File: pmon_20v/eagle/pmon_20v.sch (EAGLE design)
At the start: 34 parts, among them J1 USB, J2 MOLEX 43650-0200, J3 MOLEX 43650-0200, J4 PINHD-2X3, Q1 16Mhz, U1 LTC2943, U2 FT232RL, U3 ATMEGA328TQFP32, U4 TA48M04F

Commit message: Performed final routing.
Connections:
- net +5V renamed VIN
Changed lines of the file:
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@@
 </segment>
 </net>
-<net name="+5V" class="0">
+<net name="VIN" class="0">
 <segment>
 <wire x1="17.78" y1="205.74" x2="35.56" y2="205.74" width="0.4064" layer="91"/>

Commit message: Final tweaks.
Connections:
- net N$22 renamed VOUT
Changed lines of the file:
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@@
 <pinref part="GND21" gate="1" pin="GND"/>
 <pinref part="J2" gate="-2" pin="S"/>
+<label x="-2.54" y="190.5" size="1.778" layer="95"/>
 </segment>
 <segment>
@@
 <wire x1="55.88" y1="190.5" x2="55.88" y2="185.42" width="0.4064" layer="91"/>
 <pinref part="J3" gate="-2" pin="S"/>
+<label x="58.42" y="190.5" size="1.778" layer="95"/>
 </segment>
 <segment>
@@
 <pinref part="R4" gate="G$1" pin="I2"/>
 <pinref part="J2" gate="-1" pin="S"/>
+<label x="-2.54" y="200.66" size="1.778" layer="95"/>
 </segment>
 <segment>
@@
 </segment>
 </net>
-<net name="N$22" class="0">
+<net name="VOUT" class="0">
 <segment>
 <wire x1="48.26" y1="205.74" x2="55.88" y2="205.74" width="0.4064" layer="91"/>
@@
 <pinref part="R4" gate="G$1" pin="I1"/>
 <pinref part="J3" gate="-1" pin="S"/>
-</segment>
-</net>
+<label x="58.42" y="200.66" size="1.778" layer="95"/>
+</segment>
+</net>

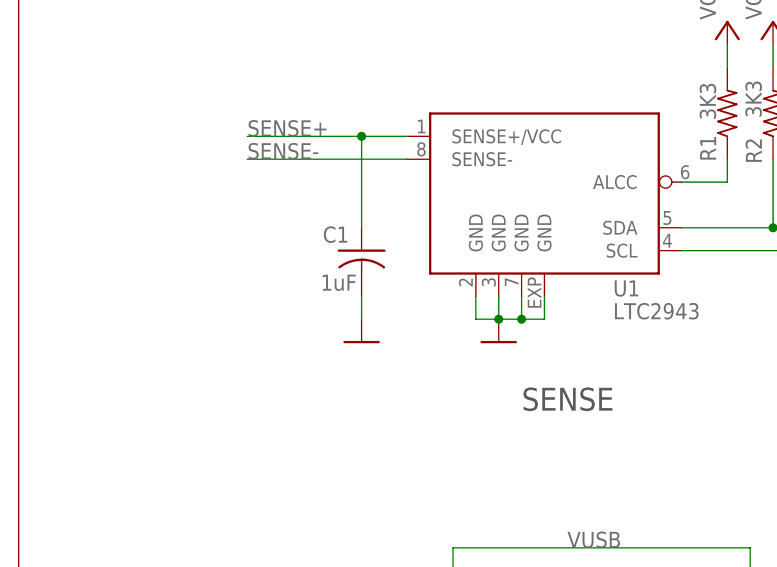
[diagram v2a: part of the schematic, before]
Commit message: Added covers for pmon 20V
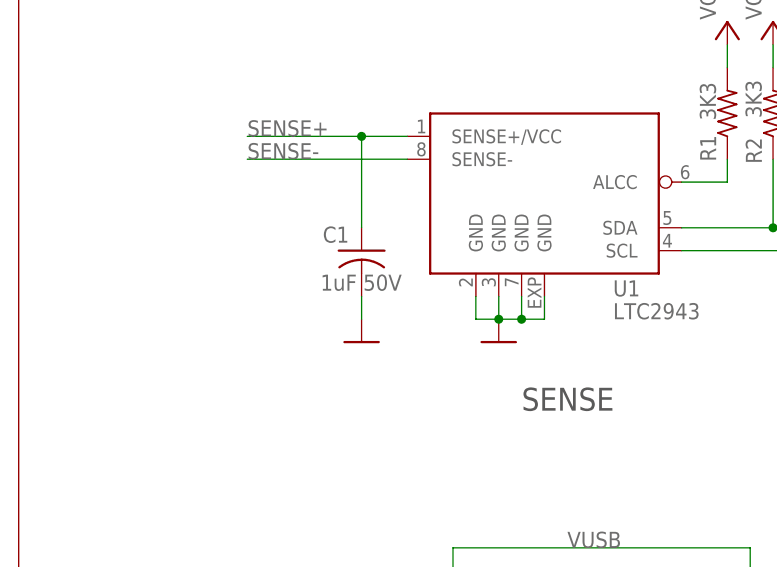
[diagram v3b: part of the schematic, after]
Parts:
- C1: value 1uF -> 1uF 50V
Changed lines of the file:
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@@
 <part name="GND23" library="pmon_20v" deviceset="GND" device=""/>
 <part name="C5" library="pmon_20v" deviceset="CAP-" device="C0603" value="0.1uF 50V"/>
-<part name="C1" library="pmon_20v" deviceset="CAP-" device="C0603" value="1uF"/>
+<part name="C1" library="pmon_20v" deviceset="CAP-" device="C0603" value="1uF 50V"/>
 <part name="R4" library="pmon_20v" deviceset="RES-SHUNT-" device="6432" value="0.025R 1%"/>
 <part name="R2" library="pmon_20v" deviceset="RES-" device="R0603" value="3K3"/>
